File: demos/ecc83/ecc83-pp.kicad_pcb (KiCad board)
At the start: 2 copper layers, 44.5 x 45.7 mm, 15 parts, among them P1 IN, P2 OUT, P3 POWER, P4 CONN_2, P5 CONN_1, P6 CONN_1, P7 CONN_1, P8 CONN_1, U1 ECC83

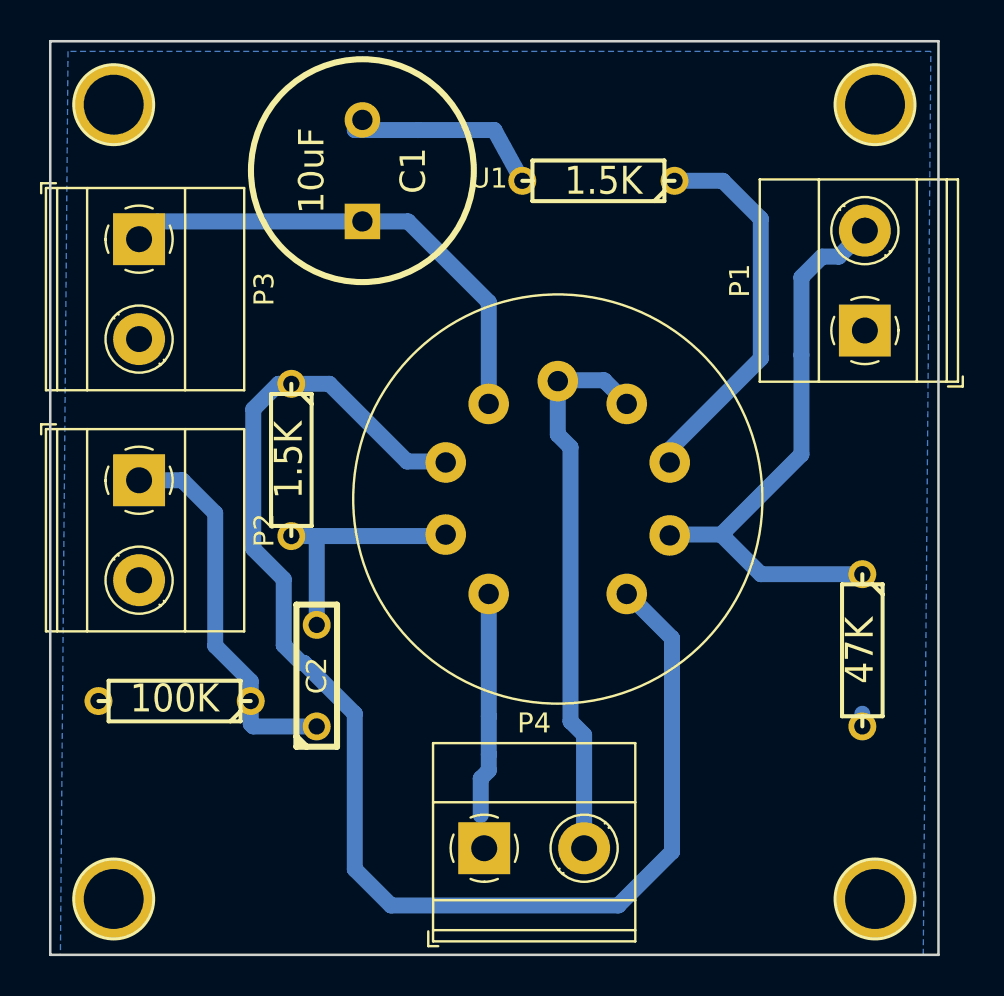
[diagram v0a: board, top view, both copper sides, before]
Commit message: hacking the toporouter. not planning to integrate it, but the algorithm is quite interesting
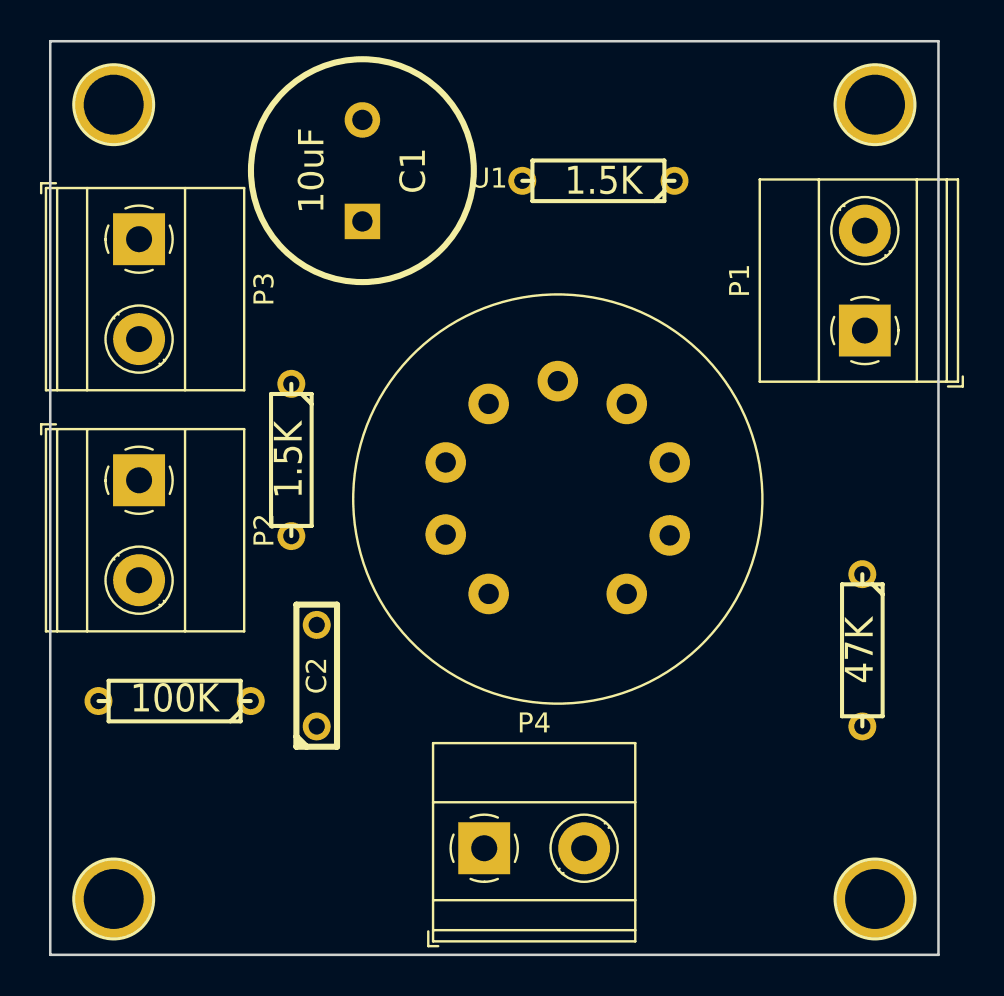
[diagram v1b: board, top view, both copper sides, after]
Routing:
- net Net-(R1-Pad1): track 68.6 -> 0.00 mm
- net Net-(P1-Pad2): track 29.1 -> 0.00 mm
- net Net-(P4-Pad2): track 27.9 -> 0.00 mm
- net Net-(C1-Pad1): track 24.6 -> 0.00 mm
- net Net-(R2-Pad1): track 19.1 -> 0.00 mm
- net Net-(C2-Pad1): track 19.1 -> 0.00 mm
- net Net-(C2-Pad2): track 12.2 -> 0.00 mm
- net Net-(P4-Pad1): track 11.3 -> 0.00 mm
- net GND: track 11.2 -> 0.00 mm
- removed copper zone on B.Cu, net GND
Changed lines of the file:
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@@
-(kicad_pcb (version 20171130) (host pcbnew "(5.0.0-rc2-151-g11ab8f6dc)")
+(kicad_pcb (version 20171130) (host pcbnew "(5.1.0-rc1-141-gfcbcdb44b-dirty)")
   (general
     (thickness 1.6002)
     (drawings 4)
-    (tracks 66)
+    (tracks 0)
     (zones 0)
     (modules 15)
@@
     (zone_45_only no)
     (trace_min 0.2)
-    (segment_width 0.381)
-    (edge_width 0.381)
     (via_size 1.2)
     (via_drill 0.6)
@@
     (uvia_min_size 0.508)
     (uvia_min_drill 0.127)
+    (edge_width 0.381)
+    (segment_width 0.381)
     (pcb_text_width 0.3048)
     (pcb_text_size 1.524 2.032)
@@
   (gr_line (start 168.275 90.805) (end 168.275 136.525) (angle 90) (layer Edge.Cuts) (width 0.127))
   (gr_line (start 123.825 90.805) (end 123.825 136.525) (angle 90) (layer Edge.Cuts) (width 0.127))
-  (segment (start 142.24 95.25) (end 146.05 95.25) (width 0.8) (layer bottom_cu) (net 1))
-  (segment (start 164.465 125.095) (end 164.465 124.46) (width 0.8) (layer bottom_cu) (net 1) (status 800))
-  (segment (start 147.447 97.79) (end 146.05 95.25) (width 0.8) (layer bottom_cu) (net 1) (status 10))
-  (segment (start 139.065 95.25) (end 142.24 95.25) (width 0.8) (layer bottom_cu) (net 1))
-  (segment (start 139.446 94.742) (end 139.065 95.25) (width 0.8) (layer bottom_cu) (net 1) (status 810))
-  (segment (start 139.446 99.822) (end 129.159 99.822) (width 0.8) (layer bottom_cu) (net 2))
-  (segment (start 129.159 99.822) (end 128.27 100.711) (width 0.8) (layer bottom_cu) (net 2))
-  (segment (start 145.7706 108.91012) (end 145.7706 103.8606) (width 0.8) (layer bottom_cu) (net 2))
-  (segment (start 145.7706 103.8606) (end 141.732 99.822) (width 0.8) (layer bottom_cu) (net 2))
-  (segment (start 141.732 99.822) (end 139.446 99.822) (width 0.8) (layer bottom_cu) (net 2))
-  (segment (start 132.08 121.059172) (end 132.08 114.4224) (width 0.8) (layer bottom_cu) (net 3))
-  (segment (start 132.08 114.4224) (end 130.4336 112.776) (width 0.8) (layer bottom_cu) (net 3))
-  (segment (start 130.4336 112.776) (end 128.27 112.776) (width 0.8) (layer bottom_cu) (net 3))
-  (segment (start 133.858 123.825) (end 133.858 122.837172) (width 0.8) (layer bottom_cu) (net 3))
-  (segment (start 133.858 122.837172) (end 132.08 121.059172) (width 0.8) (layer bottom_cu) (net 3))
-  (segment (start 133.985 125.095) (end 133.858 124.968) (width 0.8) (layer bottom_cu) (net 3))
-  (segment (start 133.858 124.968) (end 133.858 123.825) (width 0.8) (layer bottom_cu) (net 3))
-  (segment (start 137.16 125.095) (end 133.985 125.095) (width 0.8) (layer bottom_cu) (net 3))
-  (segment (start 137.16 120.015) (end 137.16 115.57) (width 0.8) (layer bottom_cu) (net 4))
-  (segment (start 135.89 115.57) (end 137.16 115.57) (width 0.8) (layer bottom_cu) (net 4))
-  (segment (start 137.16 115.57) (end 143.49984 115.57) (width 0.8) (layer bottom_cu) (net 4))
-  (segment (start 143.49984 115.57) (end 143.61668 115.45316) (width 0.8) (layer bottom_cu) (net 4))
-  (segment (start 162.450001 101.582999) (end 161.417 102.616) (width 0.8) (layer bottom_cu) (net 5))
-  (segment (start 161.417 102.616) (end 161.417 106.506) (width 0.8) (layer bottom_cu) (net 5))
-  (segment (start 164.592 100.283) (end 163.292001 101.582999) (width 0.8) (layer bottom_cu) (net 5))
-  (segment (start 163.292001 101.582999) (end 162.450001 101.582999) (width 0.8) (layer bottom_cu) (net 5))
-  (segment (start 161.417 106.506) (end 161.417 111.4806) (width 0.8) (layer bottom_cu) (net 5))
-  (segment (start 161.417 111.4806) (end 157.4038 115.4938) (width 0.8) (layer bottom_cu) (net 5))
-  (segment (start 159.385 117.475) (end 164.465 117.475) (width 0.8) (layer bottom_cu) (net 5) (status 400))
-  (segment (start 154.83332 115.4938) (end 157.4038 115.4938) (width 0.8) (layer bottom_cu) (net 5) (status 800))
-  (segment (start 157.4038 115.4938) (end 159.385 117.475) (width 0.8) (layer bottom_cu) (net 5))
-  (segment (start 145.7706 118.41988) (end 145.7706 124.587) (width 0.8) (layer bottom_cu) (net 6))
-  (segment (start 145.7706 124.587) (end 145.7706 126.492) (width 0.8) (layer bottom_cu) (net 6))
-  (segment (start 145.368 129.54) (end 145.368 127.701523) (width 0.8) (layer bottom_cu) (net 6))
-  (segment (start 145.368 127.701523) (end 145.7706 127.298923) (width 0.8) (layer bottom_cu) (net 6))
-  (segment (start 145.7706 127.298923) (end 145.7706 126.492) (width 0.8) (layer bottom_cu) (net 6))
-  (segment (start 149.86 111.125) (end 149.86 124.841) (width 0.8) (layer bottom_cu) (net 7))
-  (segment (start 150.542 131.191) (end 150.542 125.523) (width 0.8) (layer bottom_cu) (net 7))
-  (segment (start 150.542 125.523) (end 149.86 124.841) (width 0.8) (layer bottom_cu) (net 7))
-  (segment (start 149.225 110.49) (end 149.86 111.125) (width 0.8) (layer bottom_cu) (net 7))
-  (segment (start 149.225 107.7722) (end 149.225 110.49) (width 0.8) (layer bottom_cu) (net 7) (status 800))
-  (segment (start 149.225 107.7722) (end 151.54148 107.7722) (width 0.8) (layer bottom_cu) (net 7) (status 800))
-  (segment (start 151.54148 107.7722) (end 152.6794 108.91012) (width 0.8) (layer bottom_cu) (net 7) (status 400))
-  (segment (start 139.065 132.240853) (end 140.879459 134.055312) (width 0.8) (layer bottom_cu) (net 8))
-  (segment (start 135.509 121.031) (end 136.398 121.92) (width 0.8) (layer bottom_cu) (net 8))
-  (segment (start 139.065 124.46) (end 139.065 132.240853) (width 0.8) (layer bottom_cu) (net 8))
-  (segment (start 135.89 107.95) (end 135.255 107.95) (width 0.8) (layer bottom_cu) (net 8))
-  (segment (start 136.525 121.92) (end 139.065 124.46) (width 0.8) (layer bottom_cu) (net 8))
-  (segment (start 135.255 107.95) (end 133.985 109.22) (width 0.8) (layer bottom_cu) (net 8))
-  (segment (start 136.398 121.92) (end 136.525 121.92) (width 0.8) (layer bottom_cu) (net 8))
-  (segment (start 135.509 117.729) (end 135.509 121.031) (width 0.8) (layer bottom_cu) (net 8))
-  (segment (start 133.985 109.22) (end 133.985 116.205) (width 0.8) (layer bottom_cu) (net 8))
-  (segment (start 133.985 116.205) (end 135.509 117.729) (width 0.8) (layer bottom_cu) (net 8))
-  (segment (start 140.879459 134.055312) (end 152.250834 134.055312) (width 0.8) (layer bottom_cu) (net 8))
-  (segment (start 152.250834 134.055312) (end 154.94 131.366146) (width 0.8) (layer bottom_cu) (net 8))
-  (segment (start 154.94 131.366146) (end 154.94 120.68048) (width 0.8) (layer bottom_cu) (net 8))
-  (segment (start 154.94 120.68048) (end 152.6794 118.41988) (width 0.8) (layer bottom_cu) (net 8))
-  (segment (start 143.61668 111.8362) (end 141.6812 111.8362) (width 0.8) (layer bottom_cu) (net 8) (status 800))
-  (segment (start 141.6812 111.8362) (end 137.795 107.95) (width 0.8) (layer bottom_cu) (net 8))
-  (segment (start 135.89 107.95) (end 137.795 107.95) (width 0.8) (layer bottom_cu) (net 8) (status 800))
-  (segment (start 154.94 121.31548) (end 154.94 121.31548) (width 0.8) (layer bottom_cu) (net 8))
-  (segment (start 154.83332 111.8362) (end 154.83332 111.23168) (width 0.8) (layer bottom_cu) (net 9) (status 800))
-  (segment (start 159.385 106.68) (end 159.385 99.695) (width 0.8) (layer bottom_cu) (net 9))
-  (segment (start 154.83332 111.23168) (end 159.385 106.68) (width 0.8) (layer bottom_cu) (net 9))
-  (segment (start 157.48 97.79) (end 159.385 99.695) (width 0.8) (layer bottom_cu) (net 9))
-  (segment (start 155.067 97.79) (end 157.48 97.79) (width 0.8) (layer bottom_cu) (net 9) (status 810))
-  (zone (net 1) (net_name GND) (layer bottom_cu) (hatch edge 0.508)
-    (connect_pads (clearance 0.635))
-    (min_thickness 0.381)
-    (fill yes (arc_segments 32) (thermal_gap 0.254) (thermal_bridge_width 0.50038))
-    (polygon
-      (pts
-        (xy 167.513 136.525) (xy 167.894 91.313) (xy 124.714 91.313) (xy 124.333 136.525)
-      )
-    )
-  )
 )
